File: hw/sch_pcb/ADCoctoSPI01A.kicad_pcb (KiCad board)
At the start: 2 copper layers, 70.6 x 70.6 mm, 79 parts, among them J1 +5V, J10 HEADER_1x02, J11 HEADER_2x04, J2 SATA7-67491-1030, J3 SATA7-67491-1030, J4 SATA7-67491-1030, J5 SATA7-67491-1030, J6 SAS_mini_1888174, J7 SATA7-67491-1030, J8 HEADER_1x02, J9 HEADER_1x02, M1 HOLE, M2 HOLE, M3 HOLE, M4 HOLE, U1 AFE5801, U2 LM1117MP-1,8/NO, U3 LM1117MP-3,3/NO

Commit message: Repository cleanup Update of KiCAD project version to 6.0.1.
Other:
- net class Default removed

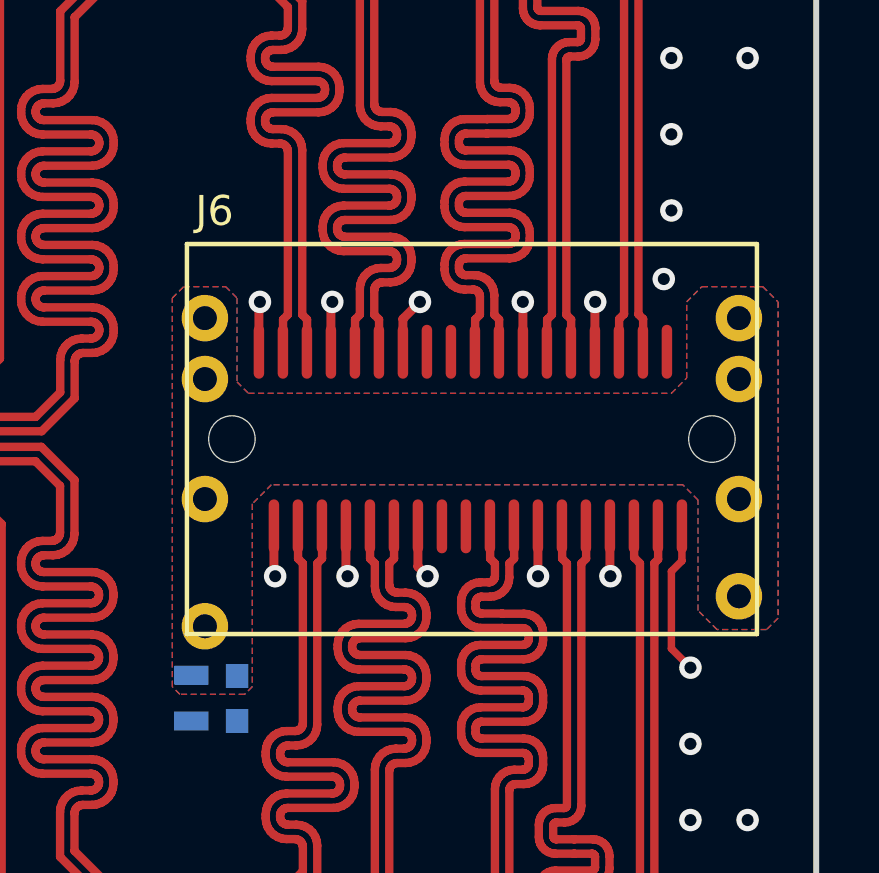
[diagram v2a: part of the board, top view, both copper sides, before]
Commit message: Update mini SAS connector footprint to up to date footprint from KiCAD library.
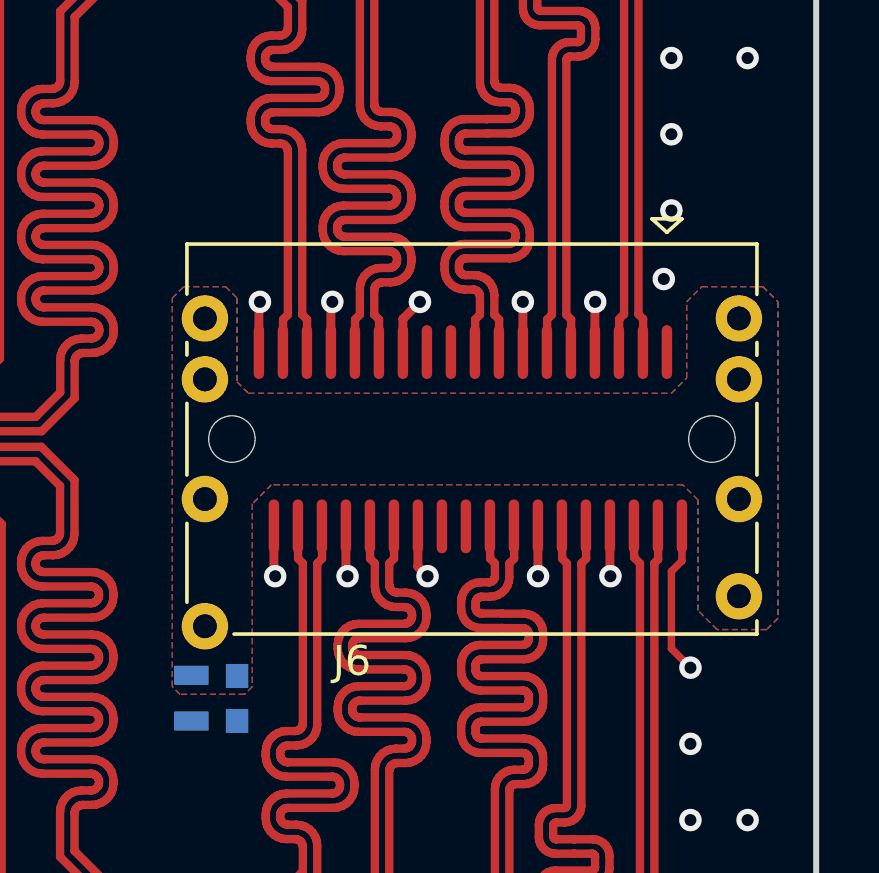
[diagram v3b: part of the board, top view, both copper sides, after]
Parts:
- J6: footprint Mlab_CON:SAS_mini_1888174 -> Connector_SATA_SAS:SAS-mini_TEConnectivity_1888174_Vertical
- R13: value 50 -> 10k
- moved J6 1.11 mm to (119.1, 102.7)
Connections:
- J6 pad A10: Net-(J6-PadA10) -> (no net)
- J6 pad A11: Net-(J6-PadA11) -> (no net)
- J6 pad B10: Net-(J6-PadB10) -> (no net)
- J6 pad B11: Net-(J6-PadB11) -> (no net)
- J7 pad 5: Net-(J7-Pad5) -> (no net)
- J7 pad 6: Net-(J7-Pad6) -> (no net)
- U1 pad 26: Net-(U1-Pad26) -> (no net)
- U1 pad 27: Net-(U1-Pad27) -> (no net)
- U1 pad 60: Net-(U1-Pad60) -> (no net)
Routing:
- net unconnected-(J7-Pad6): track 0.00 -> 0.56 mm
- net Net-(J7-Pad6): track 0.56 -> 0.00 mm
